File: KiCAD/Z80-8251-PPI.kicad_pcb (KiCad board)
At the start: 2 copper layers, 99.7 x 74.9 mm, 30 parts, among them J1 SBC8080 BUS, J2 8251-CE, J3 PPI-CE, J4 232C-CON, J5 CON-A, J6 CON-B, J7 OPM-CE, P1 Power, P2 Analog, P3 Digital, P4 Digital, P5 CONN_01X01, P6 CONN_01X01, P7 CONN_01X01, P8 CONN_01X01, Q1 2SC1815, U1 74HC138, U2 8251, U3 8255, U4 74HC4060, Y1 4.9152MHz

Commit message: PPIコネクタ再配置、電解コンデンサ追加、シルク見直し
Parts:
- added C7: 10u, Capacitor_THT:CP_Radial_D5.0mm_P2.50mm, F.Cu at (95.1, 71.1)
- Q1: footprint Package_TO_SOT_THT:TO-92_Inline -> Package_TO_SOT_THT:TO-92_Inline_Wide
- moved J5 5.59 mm to (89.3, 92.8)
- moved Q1 2.22 mm to (175.2, 80.0), turned to 270 degrees
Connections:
- J1 pad 18: Net-(J1-Pad18) -> (no net)
- J1 pad 20: Net-(J1-Pad20) -> (no net)
- J1 pad 22: Net-(J1-Pad22) -> (no net)
- J1 pad 24: Net-(J1-Pad24) -> (no net)
- J1 pad 33: Net-(J1-Pad33) -> (no net)
- J1 pad 34: Net-(J1-Pad34) -> (no net)
- J1 pad 35: Net-(J1-Pad35) -> (no net)
- J1 pad 36: Net-(J1-Pad36) -> (no net)
- J1 pad 37: Net-(J1-Pad37) -> (no net)
- J1 pad 38: Net-(J1-Pad38) -> (no net)
- J1 pad 39: Net-(J1-Pad39) -> (no net)
- J1 pad 40: Net-(J1-Pad40) -> (no net)
- J1 pad 5: Net-(J1-Pad5) -> (no net)
- J1 pad 6: Net-(J1-Pad6) -> (no net)
- J1 pad 7: Net-(J1-Pad7) -> (no net)
- J4 pad 3: Net-(J4-Pad3) -> (no net)
- J5 pad 10: PC1 -> PC5
- J5 pad 11: PC2 -> PC6
- J5 pad 12: PC3 -> PC7
- J5 pad 9: PC0 -> PC4
- J6 pad 10: PC5 -> PC1
- J6 pad 11: PC6 -> PC2
- J6 pad 12: PC7 -> PC3
- J6 pad 9: PC4 -> PC0
- P1 pad 1: Net-(P1-Pad1) -> (no net)
- P1 pad 2: Net-(P1-Pad2) -> (no net)
- P1 pad 3: Net-(P1-Pad3) -> (no net)
- P1 pad 4: Net-(P1-Pad4) -> (no net)
- P1 pad 8: Net-(P1-Pad8) -> (no net)
- P3 pad 1: Net-(P3-Pad1) -> (no net)
- P3 pad 2: Net-(P3-Pad2) -> (no net)
- P3 pad 3: Net-(P3-Pad3) -> (no net)
- P4 pad 7: Net-(P4-Pad7) -> (no net)
- P4 pad 8: Net-(P4-Pad8) -> (no net)
- P5 pad 1: Net-(P5-Pad1) -> (no net)
- P6 pad 1: Net-(P6-Pad1) -> (no net)
- P7 pad 1: Net-(P7-Pad1) -> (no net)
- P8 pad 1: Net-(P8-Pad1) -> (no net)
- U2 pad 15: Net-(U2-Pad15) -> (no net)
- U2 pad 16: Net-(U2-Pad16) -> (no net)
- U2 pad 18: Net-(U2-Pad18) -> (no net)
- U4 pad 1: Net-(U4-Pad1) -> (no net)
- U4 pad 13: Net-(U4-Pad13) -> (no net)
- U4 pad 14: Net-(U4-Pad14) -> (no net)
- U4 pad 15: Net-(U4-Pad15) -> (no net)
- U4 pad 2: Net-(U4-Pad2) -> (no net)
- U4 pad 3: Net-(U4-Pad3) -> (no net)
- U4 pad 4: Net-(U4-Pad4) -> (no net)
- U4 pad 6: Net-(U4-Pad6) -> (no net)
- U4 pad 7: Net-(U4-Pad7) -> (no net)
- U4 pad 9: Net-(U4-Pad9) -> (no net)
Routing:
- net PC6: track 6.61 -> 44.6 mm
- net PC5: track 9.77 -> 46.1 mm
- net PC4: track 7.14 -> 36.0 mm
- net PC7: track 10.4 -> 38.0 mm
- net PC2: track 44.4 -> 16.7 mm
- net PC3: track 45.6 -> 21.0 mm
- net PC1: track 37.0 -> 12.4 mm
- net PC0: track 32.8 -> 8.40 mm
- net GND: track 247.8 -> 231.5 mm
- net PA7: track 38.9 -> 27.9 mm
- net VCC: track 210.2 -> 219.6 mm
- net PA3: track 20.9 -> 28.8 mm
- net /~RESIN: track 61.7 -> 69.5 mm, vias 0 -> 2
- net PA4: track 30.5 -> 37.7 mm
- net PA2: track 12.9 -> 8.04 mm, vias 1 -> 0
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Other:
- board text added: "00"
- board text added: "20"
- board text added: "40"
- board text added: "60"
- board text added: "80"
- board text added: "A0"
- board text added: "C0"
- board text added: "CTS"
- board text added: "E0"
- board text added: "GND"
- board text added: "KZ80-IOB : Z80 I/O BOARD REV1.1"
- board text added: "NC"
- board text added: "RTS"
- board text added: "Rx"
- board text added: "Tx"
- board text added: "▽"
- board text removed: "KZ80-IOB : Z80 I/O BOARD Rev.1"

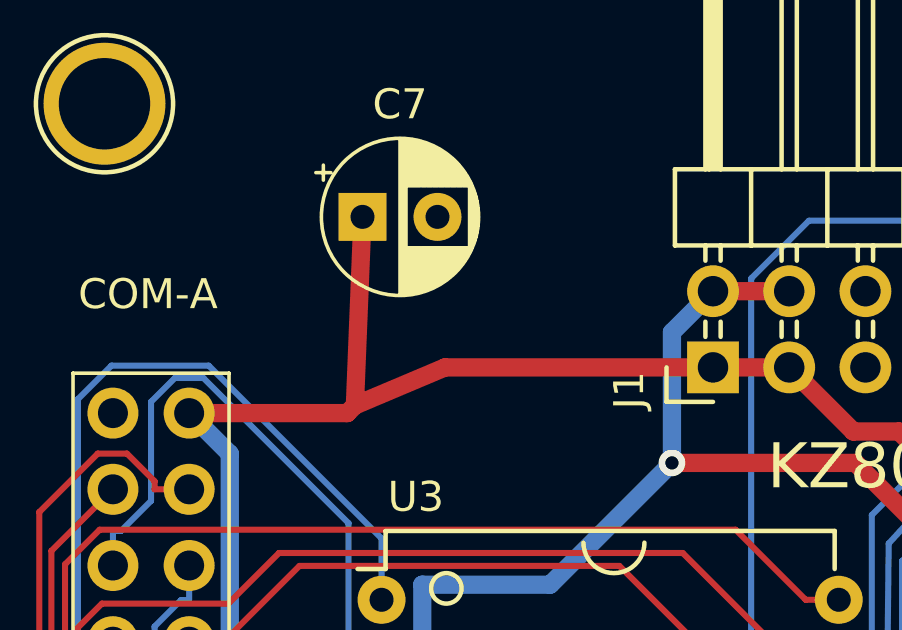
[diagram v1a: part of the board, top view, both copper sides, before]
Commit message: Rev1.1パターン見直し
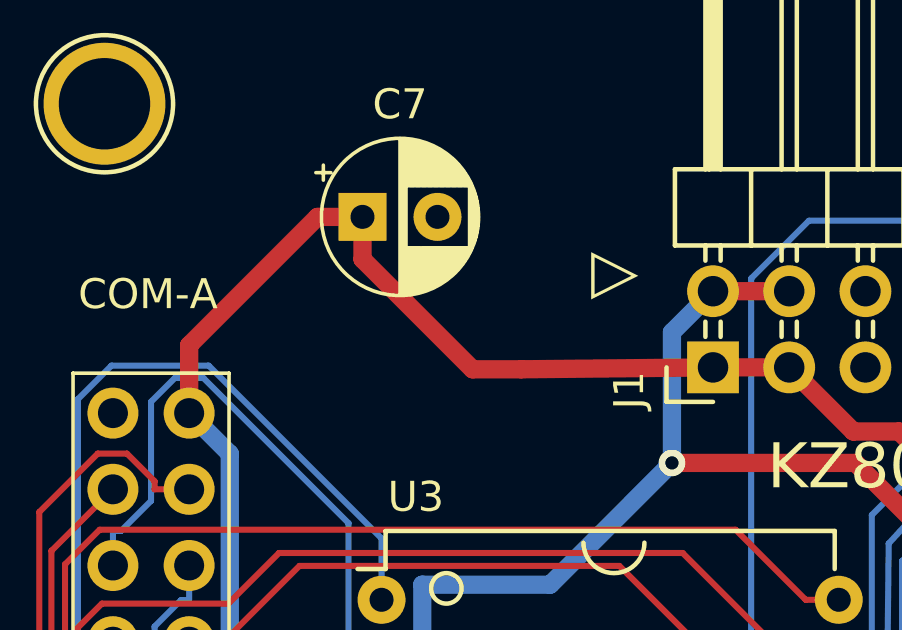
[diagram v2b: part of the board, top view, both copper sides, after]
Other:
- board text added: "▷"
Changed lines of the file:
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@@
   (general
     (thickness 1.6)
-    (drawings 36)
-    (tracks 969)
+    (drawings 37)
+    (tracks 971)
     (zones 0)
     (modules 31)
@@
     )
   )
+  (gr_text ▷ (at 103.5304 72.8599) (layer F.SilkS)
+    (effects (font (size 1.5 1.5) (thickness 0.3)))
+  )
   (gr_text E0 (at 130.413 110.435) (layer F.SilkS)
     (effects (font (size 1 1) (thickness 0.2)))
@@
   (segment (start 116.038 115.824) (end 116.038 116.84) (width 0.6096) (layer B.Cu) (net 1))
   (via (at 105.438 79.2572) (size 0.889) (layers F.Cu B.Cu) (net 1))
-  (segment (start 94.869 77.343) (end 95.123 71.0565) (width 0.6096) (layer F.Cu) (net 2))
-  (segment (start 106.807 76.073) (end 97.8751 76.073) (width 0.6096) (layer F.Cu) (net 2))
-  (segment (start 97.8751 76.073) (end 94.869 77.343) (width 0.6096) (layer F.Cu) (net 2))
   (segment (start 126.238 92.075) (end 126.238 90.7699) (width 0.6096) (layer B.Cu) (net 2))
   (segment (start 126.238 90.7699) (end 125.568 90.7699) (width 0.6096) (layer B.Cu) (net 2))
@@
   (segment (start 130.299 89.3194) (end 127.543 92.075) (width 0.6096) (layer F.Cu) (net 2))
   (segment (start 127.543 92.075) (end 126.238 92.075) (width 0.6096) (layer F.Cu) (net 2))
-  (segment (start 94.869 77.343) (end 94.615 77.597) (width 0.6096) (layer F.Cu) (net 2))
-  (segment (start 94.615 77.597) (end 89.3445 77.597) (width 0.6096) (layer F.Cu) (net 2))
   (segment (start 124.333 89.535) (end 113.008 78.2095) (width 0.6096) (layer F.Cu) (net 2))
   (segment (start 113.008 78.2095) (end 111.484 78.2095) (width 0.6096) (layer F.Cu) (net 2))
@@
   (segment (start 90.6997 104.668) (end 89.408 105.96) (width 0.6096) (layer B.Cu) (net 2))
   (segment (start 89.408 105.96) (end 89.408 107.315) (width 0.6096) (layer B.Cu) (net 2))
+  (segment (start 106.807 76.073) (end 100.4189 76.1365) (width 0.6096) (layer F.Cu) (net 2))
+  (segment (start 95.123 72.4661) (end 95.123 71.0565) (width 0.6096) (layer F.Cu) (net 2))
+  (segment (start 98.7934 76.1365) (end 95.123 72.4661) (width 0.6096) (layer F.Cu) (net 2))
+  (segment (start 100.4189 76.1365) (end 98.7934 76.1365) (width 0.6096) (layer F.Cu) (net 2))
+  (segment (start 89.3445 77.597) (end 89.3445 75.3364) (width 0.6096) (layer F.Cu) (net 2))
+  (segment (start 93.6244 71.0565) (end 95.123 71.0565) (width 0.6096) (layer F.Cu) (net 2))
+  (segment (start 89.3445 75.3364) (end 93.6244 71.0565) (width 0.6096) (layer F.Cu) (net 2))
   (segment (start 110.998 99.06) (end 110.998 97.9581) (width 0.2032) (layer B.Cu) (net 3))
   (segment (start 110.998 97.9581) (end 111.136 97.9581) (width 0.2032) (layer B.Cu) (net 3))

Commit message: REV2 回路図、製造データ出力
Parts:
- removed P1: Power, Socket_Arduino_Uno:Socket_Strip_Arduino_1x08
- removed P2: Analog, Socket_Arduino_Uno:Socket_Strip_Arduino_1x06
- removed P3: Digital, Socket_Arduino_Uno:Socket_Strip_Arduino_1x10
- removed P4: Digital, Socket_Arduino_Uno:Socket_Strip_Arduino_1x08
- removed P5, P6, P7, P8: CONN_01X01, Socket_Arduino_Uno:Arduino_1pin
- added C8: 0.1u, Capacitor_THT:C_Rect_L4.0mm_W2.5mm_P2.50mm, F.Cu at (135.0, 99.9)
- added C9: 0.1u, Capacitor_THT:C_Rect_L4.0mm_W2.5mm_P2.50mm, F.Cu at (133.3, 118.3)
- added J8: SP JP, Connector_PinHeader_2.54mm:PinHeader_1x02_P2.54mm_Horizontal, F.Cu at (176.7, 92.9)
- added JP1: A7_JP, Connector_PinHeader_2.54mm:PinHeader_1x03_P2.54mm_Vertical, F.Cu at (111.7, 114.3)
- added JP2: VCC_JP, Connector_PinHeader_2.54mm:PinHeader_1x03_P2.54mm_Vertical, F.Cu at (171.4, 72.8)
- added MH1: MountingHole, MountingHole:MountingHole_3.2mm_M3, F.Cu at (86.7, 67.2)
- added MH2: MountingHole, MountingHole:MountingHole_3.2mm_M3, F.Cu at (174.8, 67.2)
- added MH3: MountingHole, MountingHole:MountingHole_3.2mm_M3, F.Cu at (86.8, 133.2)
- added MH4: MountingHole, MountingHole:MountingHole_3.2mm_M3, F.Cu at (174.8, 133.3)
- added R4: 100k, Resistor_THT:R_Axial_DIN0207_L6.3mm_D2.5mm_P10.16mm_Horizontal, F.Cu at (170.3, 110.0)
- added R5: 100k, Resistor_THT:R_Axial_DIN0207_L6.3mm_D2.5mm_P10.16mm_Horizontal, F.Cu at (174.0, 110.0)
- added R6: 100k, Resistor_THT:R_Axial_DIN0207_L6.3mm_D2.5mm_P10.16mm_Horizontal, F.Cu at (177.3, 110.0)
- added U5: 8259, Package_DIP:DIP-28_W15.24mm_Socket, F.Cu at (136.6, 133.9)
- added U6: 8254, Package_DIP:DIP-24_W15.24mm_Socket, F.Cu at (138.4, 115.0)
- C1, C2, C3, C4, C5, C6: footprint Capacitors_THT:C_Rect_L4.0mm_W2.5mm_P2.50mm -> Capacitor_THT:C_Rect_L4.0mm_W2.5mm_P2.50mm
- J2: value 8251-CE -> ADDR_JP; footprint Pin_Headers:Pin_Header_Straight_2x08 -> Connector_PinHeader_2.54mm:PinHeader_2x04_P2.54mm_Vertical
- J3: value PPI-CE -> IR JP; footprint Pin_Headers:Pin_Header_Straight_2x08 -> Connector_PinHeader_2.54mm:PinHeader_1x05_P2.54mm_Horizontal
- J4: footprint Pin_Headers:Pin_Header_Angled_1x06 -> Connector_PinHeader_2.54mm:PinHeader_1x06_P2.54mm_Horizontal
- J5, J6: footprint Pin_Headers:Pin_Header_Straight_2x07_Pitch2.54mm -> Connector_PinHeader_2.54mm:PinHeader_2x07_P2.54mm_Vertical
- J7: value OPM-CE -> SERIAL JP; footprint Pin_Headers:Pin_Header_Straight_2x08 -> Connector_PinHeader_2.54mm:PinHeader_2x04_P2.54mm_Vertical
- R1: footprint Resistors_THT:R_Axial_DIN0207_L6.3mm_D2.5mm_P10.16mm_Horizontal -> Resistor_THT:R_Axial_DIN0207_L6.3mm_D2.5mm_P10.16mm_Horizontal
- U1: value 74HC138 -> 74LS139; footprint Housings_DIP:DIP-16_W7.62mm_Socket -> Package_DIP:DIP-16_W7.62mm_Socket
- U2: footprint Housings_DIP:DIP-28_W15.24mm_Socket -> Package_DIP:DIP-28_W15.24mm_Socket
- U3: footprint Housings_DIP:DIP-40_W15.24mm -> Package_DIP:DIP-40_W15.24mm_Socket
- Y1: value 4.9152MHz -> 19.6608MHz
- moved Q1 77.3 mm to (110.9, 122.9), turned to 0 degrees
- moved R2 74.4 mm to (111.1, 128.7), turned to 0 degrees
- moved R3 73.5 mm to (121.3, 132.5), turned to 180 degrees
- moved J3 49.2 mm to (176.7, 115.9)
- moved J2 40.6 mm to (111.6, 109.9), turned to 90 degrees
- moved C6 35.1 mm to (135.1, 80.0), turned to 270 degrees
- moved C4 32.0 mm to (132.0, 81.3)
- moved U4 31.5 mm to (123.7, 84.5)
- moved C2 26.5 mm to (119.3, 124.0)
- moved J7 24.2 mm to (123.7, 109.9), turned to 90 degrees
- moved R1 20.9 mm to (119.2, 120.5), turned to 0 degrees
- moved U2 18.5 mm to (138.3, 95.9), turned to 90 degrees
- moved J4 16.8 mm to (176.8, 74.0)
- moved C1 15.3 mm to (129.4, 123.9), turned to 180 degrees
- moved U1 10.3 mm to (111.6, 84.5)
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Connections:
- J1 pad 1: VCC -> SBC5V
- J1 pad 18: (no net) -> Net-(J1-Pad18)
- J1 pad 20: (no net) -> Net-(J1-Pad20)
- J1 pad 22: (no net) -> Net-(J1-Pad22)
- J1 pad 24: (no net) -> Net-(J1-Pad24)
- J1 pad 27: A2 -> Net-(J1-Pad27)
- J1 pad 3: VCC -> SBC5V
- J1 pad 33: (no net) -> Net-(J1-Pad33)
- J1 pad 34: (no net) -> Net-(J1-Pad34)
- J1 pad 35: (no net) -> Net-(J1-Pad35)
- J1 pad 36: (no net) -> Net-(J1-Pad36)
- J1 pad 37: (no net) -> Net-(J1-Pad37)
- J1 pad 38: (no net) -> Net-(J1-Pad38)
- J1 pad 39: (no net) -> Net-(J1-Pad39)
- J1 pad 40: (no net) -> Net-(J1-Pad40)
- J1 pad 5: (no net) -> ~INTA
- J1 pad 6: (no net) -> Net-(J1-Pad6)
- J1 pad 7: (no net) -> Net-(J1-Pad7)
- J2 pad 2: Net-(J2-Pad10) -> Net-(J2-Pad2)
- J2 pad 4: Net-(J2-Pad10) -> Net-(J2-Pad2)
- J2 pad 6: Net-(J2-Pad10) -> Net-(J2-Pad2)
- J2 pad 8: Net-(J2-Pad10) -> Net-(J2-Pad2)
- J3 pad 1: Net-(J2-Pad1) -> /IR6
- J3 pad 2: Net-(J3-Pad10) -> /IR3
- J3 pad 3: Net-(J2-Pad3) -> /IR2
- J3 pad 4: Net-(J3-Pad10) -> /IR1
- J3 pad 5: Net-(J2-Pad5) -> /IR0
- J4 pad 3: (no net) -> Net-(J4-Pad3)
- J7 pad 1: Net-(J2-Pad1) -> Net-(J7-Pad1)
- J7 pad 2: ~CE -> Net-(J7-Pad2)
- J7 pad 3: Net-(J2-Pad3) -> Net-(J7-Pad1)
- J7 pad 4: ~CE -> Net-(J7-Pad4)
- J7 pad 5: Net-(J2-Pad5) -> Net-(J7-Pad1)
- J7 pad 6: ~CE -> Net-(J7-Pad6)
- J7 pad 7: Net-(J2-Pad7) -> Net-(J7-Pad1)
- J7 pad 8: ~CE -> Net-(J7-Pad8)
- Q1 pad 2: /~RESIN -> Net-(JP1-Pad1)
- R2 pad 2: RES -> A7
- R3 pad 1: VCC -> Net-(JP1-Pad1)
- R3 pad 2: /~RESIN -> VCC
- U1 pad 1: A5 -> Net-(J2-Pad2)
- U1 pad 10: Net-(J2-Pad11) -> Net-(J2-Pad5)
- U1 pad 11: Net-(J2-Pad9) -> Net-(J2-Pad3)
- U1 pad 12: Net-(J2-Pad7) -> Net-(J2-Pad1)
- U1 pad 13: Net-(J2-Pad5) -> A6
- U1 pad 14: Net-(J2-Pad3) -> A5
- U1 pad 15: Net-(J2-Pad1) -> Net-(JP1-Pad2)
- U1 pad 2: A6 -> A3
- U1 pad 3: A7 -> A4
- U1 pad 4: GND -> 8251A-CS
- U1 pad 5: GND -> 8255-CS
- U1 pad 6: VCC -> 8259-CS
- U1 pad 7: Net-(J2-Pad15) -> 8254-CS
- U1 pad 9: Net-(J2-Pad13) -> Net-(J2-Pad7)
- U2 pad 11: Net-(J2-Pad10) -> 8251A-CS
- U2 pad 14: INT -> 8251-A
- U2 pad 15: (no net) -> Net-(U2-Pad15)
- U2 pad 16: (no net) -> Net-(U2-Pad16)
- U2 pad 18: (no net) -> Net-(U2-Pad18)
- U2 pad 25: Net-(U2-Pad25) -> Net-(J7-Pad1)
- U2 pad 9: Net-(U2-Pad25) -> Net-(J7-Pad1)
- U3 pad 6: Net-(J3-Pad10) -> 8255-CS
- U4 pad 1: (no net) -> Net-(U4-Pad1)
- U4 pad 13: (no net) -> Net-(U4-Pad13)
- U4 pad 14: (no net) -> Net-(U4-Pad14)
- U4 pad 15: (no net) -> Net-(U4-Pad15)
- U4 pad 2: (no net) -> Net-(U4-Pad2)
- U4 pad 3: (no net) -> Net-(U4-Pad3)
- U4 pad 4: (no net) -> Net-(J7-Pad6)
- U4 pad 5: Net-(U2-Pad25) -> Net-(J7-Pad4)
- U4 pad 6: (no net) -> Net-(J7-Pad8)
- U4 pad 7: (no net) -> Net-(J7-Pad2)
- U4 pad 9: (no net) -> Net-(U4-Pad9)
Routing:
- net VCC: track 219.9 -> 368.0 mm, vias 0 -> 2
- net ~IOR: track 112.0 -> 229.8 mm, vias 1 -> 0
- net GND: track 231.5 -> 334.3 mm, vias 1 -> 5
- net 8259-CS: track 0.00 -> 87.2 mm
- net ~INTA: track 0.00 -> 80.7 mm, vias 0 -> 1
- net A5: track 108.5 -> 32.2 mm, vias 1 -> 0
- net A4: track 110.1 -> 37.6 mm
- net Net-(J7-Pad2): track 0.00 -> 70.9 mm
- net SBC5V: track 0.00 -> 70.5 mm
- net A2: track 69.7 -> 0.00 mm
- net /~RESIN: track 69.5 -> 0.00 mm, vias 2 -> 0
- net Net-(U2-Pad25): track 64.0 -> 0.00 mm
- net A3: track 99.5 -> 36.7 mm
- net Net-(J7-Pad1): track 0.00 -> 62.0 mm
- net Net-(J3-Pad10): track 60.3 -> 0.00 mm
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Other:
- net class BOLD: trace_width 0.6096 -> 0.6; via_dia 0.889 -> 0.8; via_drill 0.635 -> 0.4
- net class Default: trace_width 0.2032 -> 0.25; via_dia 0.889 -> 0.8; via_drill 0.635 -> 0.4
- rule via_min_drill: 0.06096 -> 0.4
- rule via_min_size: 0.889 -> 0.8
- board text added: "19"
- board text added: "38"
- board text added: "5V"
- board text added: "74HC139"
- board text added: "76"
- board text added: "8080BUS"
- board text added: "8251 (USART)"
- board text added: "8254 (PIT)"
- board text added: "8255 (PPI)"
- board text added: "8259 (PIC)"
- board text added: "9"
- board text added: "FTDN"
- board text added: "IR0"
- board text added: "IR1"
- board text added: "IR2"
- board text added: "IR3"
- board text added: "IR6"
- board text added: "KZ80-IOB REV2"
- board text added: "POWER"
- board text added: "SBC8080 BUS"
- board text added: "SP JP"
- board text added: "Z80 I/O BOARD"
- board text removed: "1"
- board text removed: "232C"
- board text removed: "74HC138"
- board text removed: "8251"
- board text removed: "8255"
- board text removed: "A0"
- board text removed: "C0"
- board text removed: "E0"
- board text removed: "KZ80-IOB : Z80 I/O BOARD REV1.1"
- board text removed: "NC"
- board text removed: "OPM"
- board text removed: "PPI"

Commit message: REV3 回路図、パターン検討 その1
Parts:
- added C10: 22p, Capacitor_THT:C_Disc_D3.0mm_W1.6mm_P2.50mm, F.Cu at (129.7, 128.3)
- added JP3: G0 JP, Jumper:SolderJumper-2_P1.3mm_Open_RoundedPad1.0x1.5mm, B.Cu at (159.0, 103.3)
- added JP4: G1 JP, Jumper:SolderJumper-2_P1.3mm_Open_RoundedPad1.0x1.5mm, B.Cu at (159.2, 107.3)
- added JP5: G2 JP, Jumper:SolderJumper-2_P1.3mm_Open_RoundedPad1.0x1.5mm, B.Cu at (159.2, 111.3)
- added JP6: 8254-1JP, Jumper:SolderJumper-3_P1.3mm_Bridged12_RoundedPad1.0x1.5mm, B.Cu at (143.2, 109.3)
- added JP7: 8254-1JP, Jumper:SolderJumper-3_P1.3mm_Bridged12_RoundedPad1.0x1.5mm, B.Cu at (143.2, 104.3)
- C1, C2, C3, C4, C5, C6, C8, C9: footprint Capacitor_THT:C_Rect_L4.0mm_W2.5mm_P2.50mm -> Capacitor_THT:C_Disc_D3.0mm_W1.6mm_P2.50mm
- JP2: value VCC_JP -> USB POWER; footprint Connector_PinHeader_2.54mm:PinHeader_1x03_P2.54mm_Vertical -> Jumper:SolderJumper-2_P1.3mm_Open_RoundedPad1.0x1.5mm
- moved JP2 4.98 mm to (167.2, 75.3), turned to 180 degrees
- moved MH2 0.83 mm to (175.7, 67.2)
- moved J1 0.48 mm to (106.8, 75.6)
- moved C1 0.46 mm to (129.7, 124.3)
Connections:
- net Net-(R4-Pad2) renamed G0
- net Net-(R5-Pad2) renamed G1
- net Net-(R6-Pad2) renamed G2
- J1 pad 1: SBC5V -> VCC
- J1 pad 3: SBC5V -> VCC
- U6 pad 10: 8254-1 -> Net-(JP6-Pad2)
- U6 pad 13: 8254-2 -> Net-(JP7-Pad2)
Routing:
- net PC6: track 26.2 -> 191.1 mm, vias 0 -> 1
- net GND: track 334.3 -> 497.8 mm, vias 5 -> 6
- net PC5: track 30.9 -> 156.4 mm, vias 0 -> 1
- net PC4: track 28.9 -> 149.7 mm, vias 0 -> 1
- net SBC5V: track 70.5 -> 0.00 mm
- net D3: track 120.6 -> 169.4 mm
- net D2: track 103.3 -> 146.8 mm, vias 2 -> 1
- net VCC: track 368.0 -> 409.5 mm, vias 2 -> 6
- net Net-(JP7-Pad2): track 0.00 -> 39.2 mm, vias 0 -> 2
- net Net-(J8-Pad1): track 29.2 -> 63.4 mm, vias 0 -> 2
- net 8259-CS: track 87.2 -> 53.0 mm
- net PA5: track 61.6 -> 27.6 mm, vias 0 -> 1
- net ~IOW: track 145.6 -> 175.8 mm, vias 1 -> 2
- net D1: track 134.6 -> 164.6 mm, vias 0 -> 3
- net D4: track 120.3 -> 146.4 mm, vias 1 -> 0
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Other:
- board size 99.7 x 74.9 mm -> 100 x 74.9 mm
- board text added: "GATE0"
- board text added: "GATE1"
- board text added: "GATE2"
- board text added: "INT"
- board text added: "KZ80-IOB REV3"
- board text added: "SND"
- board text added: "USB POWER"
- board text removed: "8080BUS"
- board text removed: "FTDN"
- board text removed: "KZ80-IOB REV2"
- board text removed: "POWER"

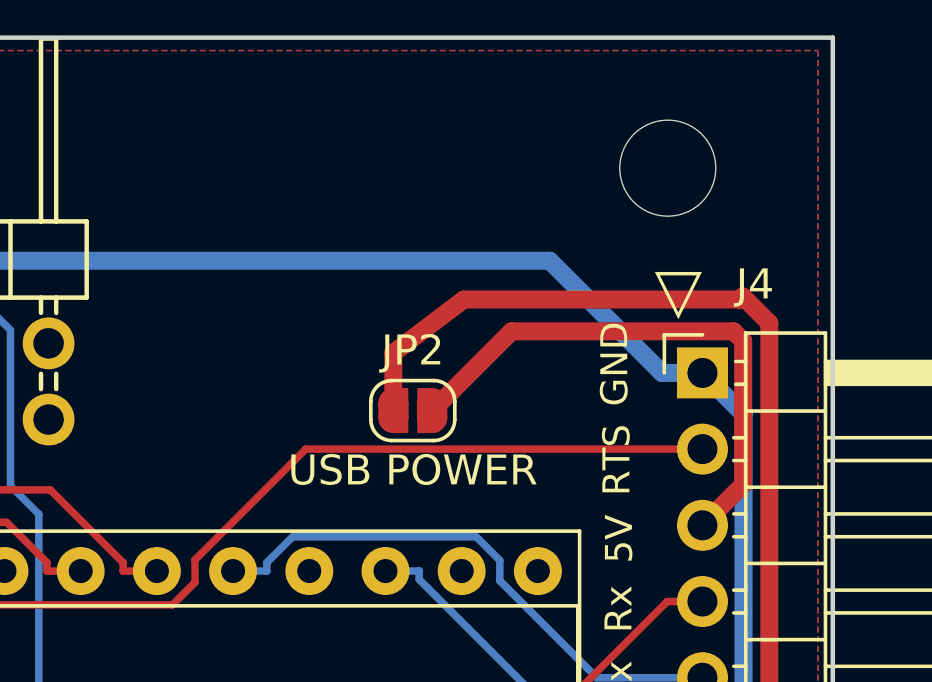
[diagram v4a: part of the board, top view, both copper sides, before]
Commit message: FTDI +5Vへダイオード追加
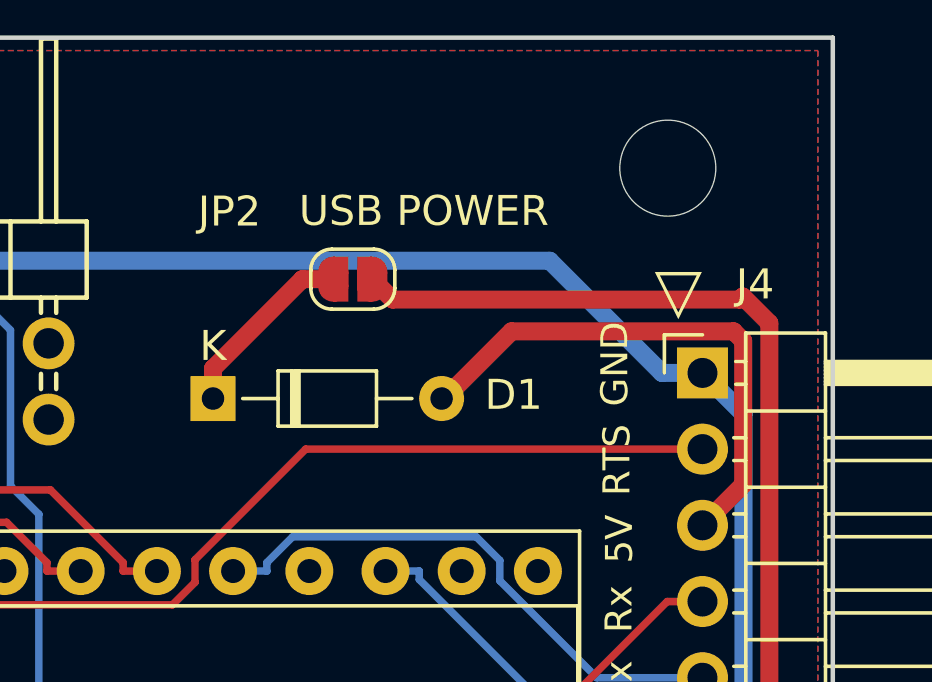
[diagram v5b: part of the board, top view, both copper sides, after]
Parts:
- added D1: 1S4, Diode_THT:D_DO-34_SOD68_P7.62mm_Horizontal, F.Cu at (160.5, 74.9)
- moved JP2 4.82 mm to (165.2, 70.9), turned to 0 degrees
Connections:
- J4 pad 3: Net-(J4-Pad3) -> Net-(D1-Pad2)
- JP2 pad 1: Net-(J4-Pad3) -> Net-(D1-Pad1)
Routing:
- net Net-(J4-Pad3): track 18.3 -> 0.00 mm
- net Net-(D1-Pad2): track 0.00 -> 17.8 mm
- net Net-(D1-Pad1): track 0.00 -> 6.24 mm
- net VCC: track 409.5 -> 407.9 mm
